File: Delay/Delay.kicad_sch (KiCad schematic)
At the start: 14 parts, among them J1 9V battery, J2 DC IN, J4 IN, J5 OUT, U1 PT2399

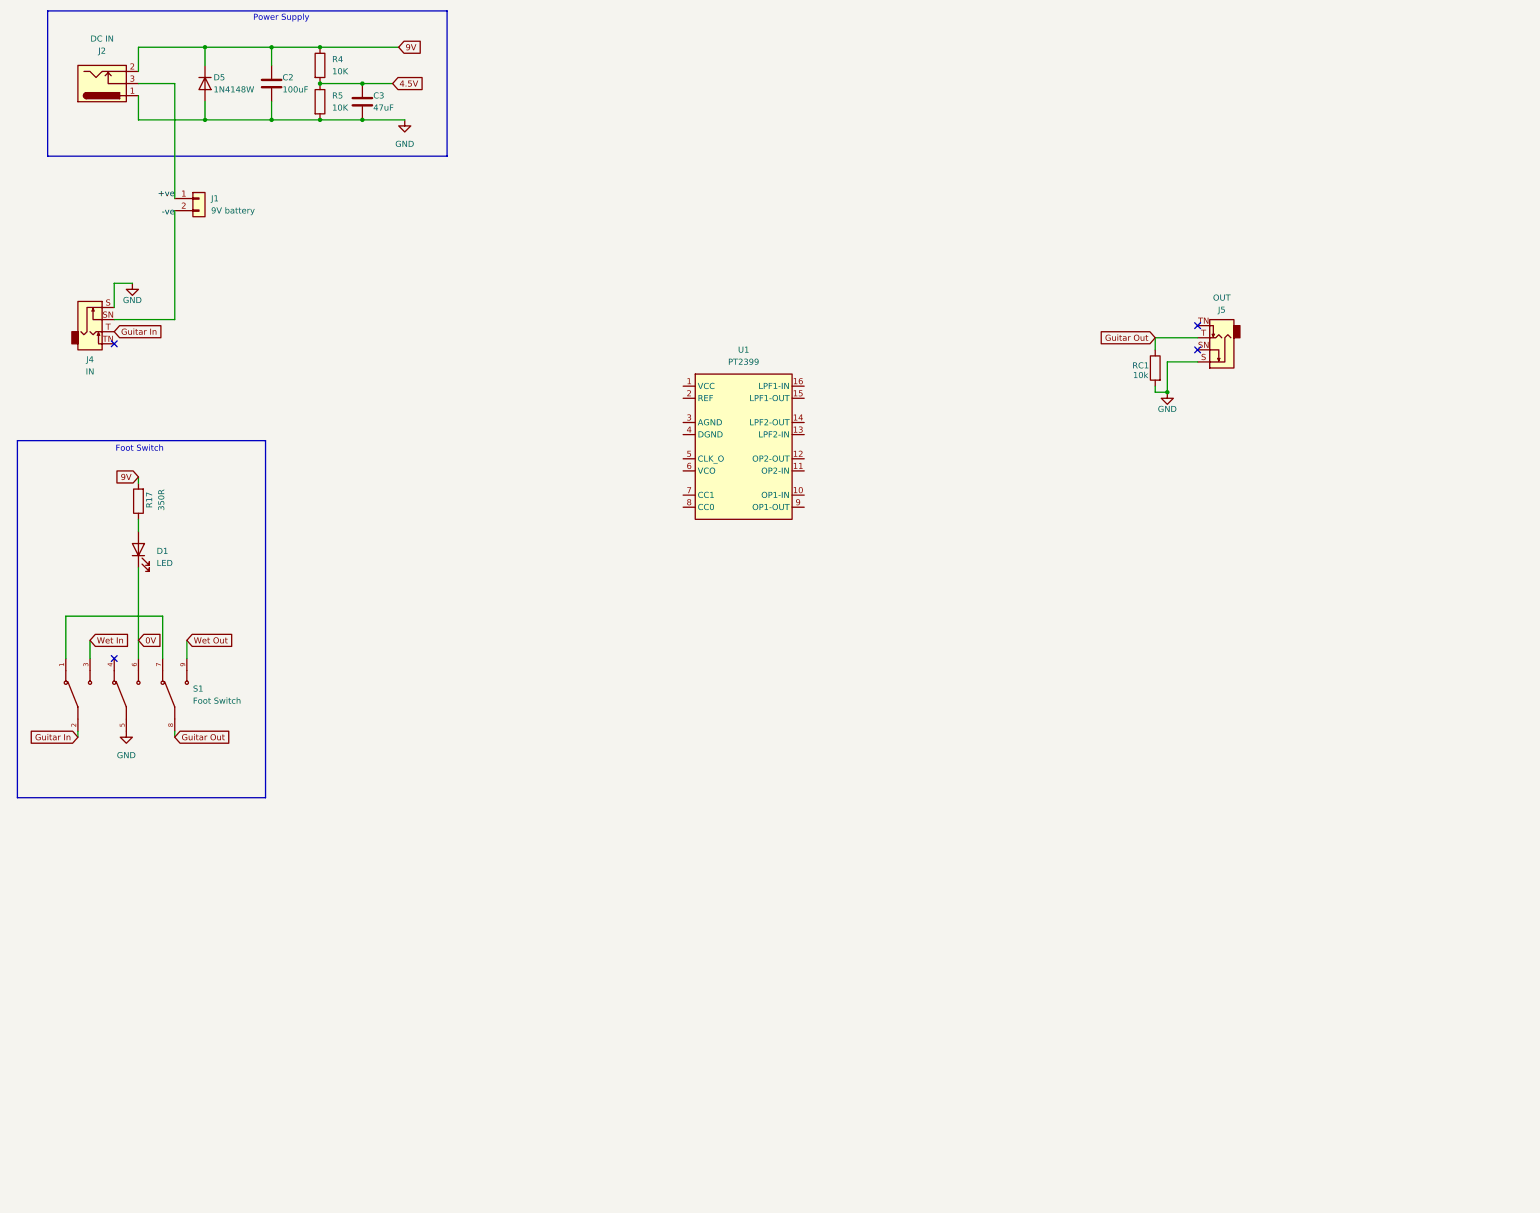
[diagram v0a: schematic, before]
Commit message: Schematic Complete. Need to finalise footprints and PCB layout.
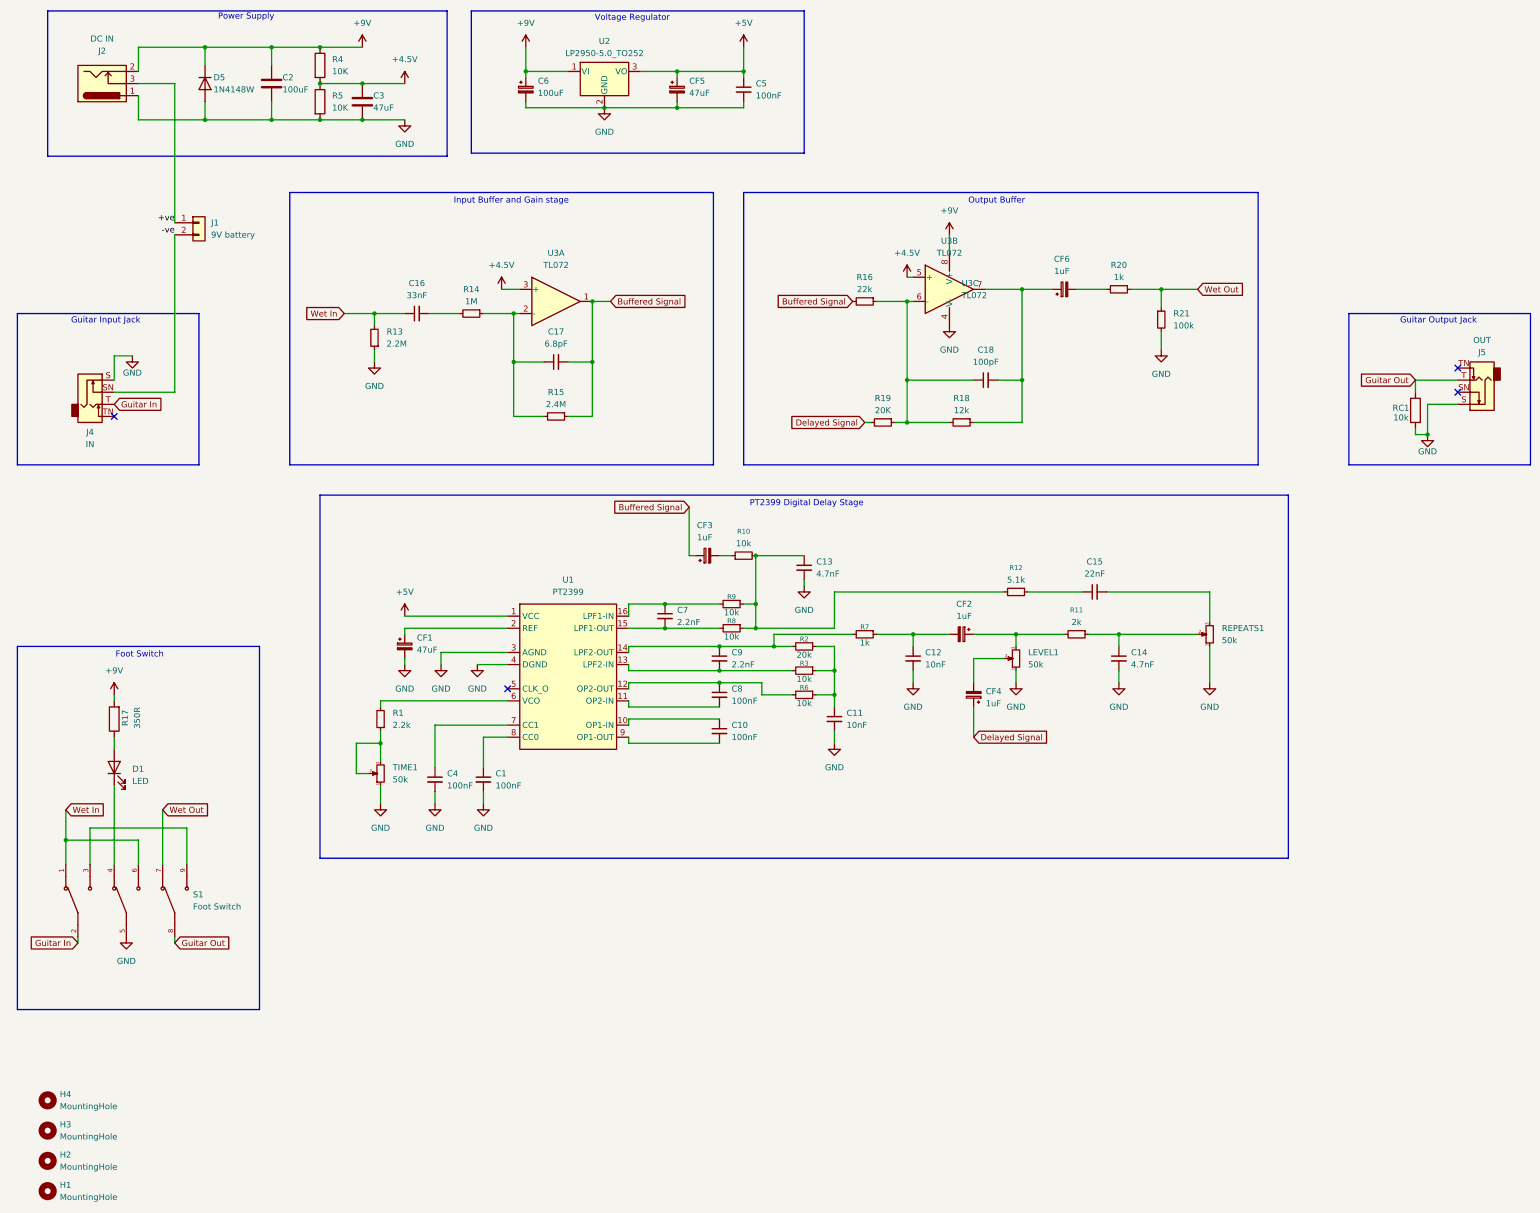
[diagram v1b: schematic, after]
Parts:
- added C1, C10, C4, C5, C8: 100nF, Capacitor_SMD:C_0805_2012Metric, symbol Device:C_Small
- added C11, C12: 10nF, Capacitor_SMD:C_0805_2012Metric, symbol Device:C_Small
- added C13, C14: 4.7nF, Capacitor_SMD:C_0805_2012Metric, symbol Device:C_Small
- added C15: 22nF, Capacitor_SMD:C_0805_2012Metric, symbol Device:C_Small
- added C16: 33nF, Capacitor_SMD:C_0805_2012Metric, symbol Device:C_Small
- added C17: 6.8pF, Capacitor_SMD:C_0805_2012Metric, symbol Device:C_Small
- added C18: 100pF, Capacitor_SMD:C_0805_2012Metric, symbol Device:C_Small
- added C6: 100uF, Capacitor_SMD:C_1206_3216Metric, symbol Device:C_Polarized_Small
- added C7, C9: 2.2nF, Capacitor_SMD:C_0805_2012Metric, symbol Device:C_Small
- added CF1, CF5: 47uF, Capacitor_SMD:CP_Elec_5x3, symbol Device:C_Polarized_Small
- added CF2, CF3, CF4, CF6: 1uF, Capacitor_SMD:CP_Elec_5x3, symbol Device:C_Polarized_Small
- added H1, H2, H3, H4: MountingHole, MountingHole:MountingHole_3.2mm_M3, symbol Mechanical:MountingHole
- added LEVEL1, REPEATS1, TIME1: 50k, Potentiometer_THT:Potentiometer_RK097_Single_Vertical, symbol Device:R_Potentiometer_Small
- added R1: 2.2k, Resistor_SMD:R_0603_1608Metric, symbol Device:R_Small
- added R10, R3, R6, R8, R9: 10k, Resistor_SMD:R_0603_1608Metric, symbol Device:R_Small
- added R11: 2k, Resistor_SMD:R_0603_1608Metric, symbol Device:R_Small
- added R12: 5.1k, Resistor_SMD:R_0603_1608Metric, symbol Device:R_Small
- added R13: 2.2M, Resistor_SMD:R_0603_1608Metric, symbol Device:R_Small
- added R14: 1M, Resistor_SMD:R_0603_1608Metric, symbol Device:R_Small
- added R15: 2.4M, Resistor_SMD:R_0603_1608Metric, symbol Device:R_Small
- added R16: 22k, Resistor_SMD:R_0603_1608Metric, symbol Device:R_Small
- added R18: 12k, Resistor_SMD:R_0603_1608Metric, symbol Device:R_Small
- added R19: 20K, Resistor_SMD:R_0603_1608Metric, symbol Device:R_Small
- added R2: 20k, Resistor_SMD:R_0603_1608Metric, symbol Device:R_Small
- added R20, R7: 1k, Resistor_SMD:R_0603_1608Metric, symbol Device:R_Small
- added R21: 100k, Resistor_SMD:R_0603_1608Metric, symbol Device:R_Small
- added U2: LP2950-5.0_TO252, Package_TO_SOT_SMD:TO-252-2, symbol Regulator_Linear:LP2950-5.0_TO252
- added U3: TL072, Package_SO:SOIC-8_5.3x6.2mm_P1.27mm, symbol Amplifier_Operational:TL072
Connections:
- net GND: now also U1.3 (AGND), U1.4 (DGND), C1.2, C11.2, C12.2, C13.2, C14.2, C4.2, C5.2, C6.2, CF1.2, CF5.2, LEVEL1.1, R13.1, R21.2, REPEATS1.1, TIME1.1, U2.2 (GND), U3.4 (V-)
- net Wet In: now also S1.1, S1.6, C16.1, R13.2; no longer S1.3
- net Wet Out: now also S1.7, R20.1, R21.1; no longer S1.9
- net at S1.4: now also D1.1 (K)
- net +5V: now reaches U1.1 (VCC)
- net +5V: now also C5.1, CF5.1, U2.3 (VO)
- net at U1.10 (OP1-IN): now also C10.1
- net at U1.11 (OP2-IN): now also C8.2
- net at U1.12 (OP2-OUT): now also C8.1, R6.2
- net at U1.13 (LPF2-IN): now also C9.2, R3.2
- net at U1.14 (LPF2-OUT): now also C9.1, R2.2, R7.2
- net at U1.15 (LPF1-OUT): now also C7.2, R8.2
- net at U1.16 (LPF1-IN): now also C7.1, R9.2
- net at U1.2 (REF): now also CF1.1
- net at U1.6 (VCO): now also R1.2
- net at U1.7 (CC1): now also C4.1
- net at U1.8 (CC0): now also C1.1
- net at U1.9 (OP1-OUT): now also C10.2
- removed net 0V: D1.1 (K), S1.6
- net 4.5V renamed +4.5V
- net +4.5V: now also U3.3 (+), U3.5 (+)
- net 9V renamed +9V
- net +9V: now also C6.1, U2.1 (VI), U3.8 (V+)
- new net: CF4.2, LEVEL1.2
- new net: CF2.1, LEVEL1.3, R11.2
- new net: C18.2, CF6.1, R18.1, U3.7
- new net: C18.1, R16.1, R18.2, R19.1, U3.6 (-)
- new net: C13.1, R10.2, R12.2, R8.1, R9.1
- new net: C14.1, R11.1, REPEATS1.2
- new net: C17.1, R14.1, R15.2, U3.2 (-)
- new net: C16.2, R14.2
- new net: C11.1, R2.1, R3.1, R6.1
- new net: R1.1, TIME1.2, TIME1.3
- new net: C15.1, R12.1
- new net: CF6.2, R20.2
- new net: C15.2, REPEATS1.3
- new net: CF3.2, R10.1
- new net: C12.1, CF2.2, R7.1
- new net: S1.3, S1.9
- new net Buffered Signal: C17.2, CF3.1, R15.1, R16.2, U3.1
- new net Delayed Signal: CF4.1, R19.2
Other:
- note added: "Guitar Input Jack"
- note added: "Guitar Output Jack"
- note added: "Input Buffer and Gain stage"
- note added: "Output Buffer"
- note added: "PT2399 Digital Delay Stage"
- note added: "Voltage Regulator"
- title: (none) -> Delay
- moved on the sheet: D1, J1, J4, J5, R17, RC1, S1, U1

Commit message: Completed PCB layout, still need to finish BOM.
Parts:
- removed J1: 9V battery, Connector_PinSocket_2.00mm:PinSocket_1x02_P2.00mm_Vertical, symbol Connector_Generic:Conn_01x02
- added +9VBATT1: 9V Batt +ve, TestPoint:TestPoint_THTPad_2.5x2.5mm_Drill1.2mm, symbol Connector:TestPoint
- added -9VBATT1: 9V Batt -ve, TestPoint:TestPoint_THTPad_2.5x2.5mm_Drill1.2mm, symbol Connector:TestPoint
- C3: renamed from C16; value 33nF -> 220nF
- C6: renamed from C17; value 6.8pF -> 47pF
- CF1: footprint Capacitor_SMD:CP_Elec_5x3 -> Capacitor_SMD:CP_Elec_6.3x7.7
- CF2: renamed from C6; footprint Capacitor_SMD:C_1206_3216Metric -> Capacitor_SMD:CP_Elec_6.3x7.7
- CF3: renamed from CF5; footprint Capacitor_SMD:CP_Elec_5x3 -> Capacitor_SMD:CP_Elec_6.3x7.7
- CF4: renamed from CF3; footprint Capacitor_SMD:CP_Elec_5x3 -> Capacitor_SMD:CP_Elec_4x5.4
- CF5: renamed from CF2; footprint Capacitor_SMD:CP_Elec_5x3 -> Capacitor_SMD:CP_Elec_4x5.4
- CF6: renamed from CF4; footprint Capacitor_SMD:CP_Elec_5x3 -> Capacitor_SMD:CP_Elec_4x5.4
- CF7: renamed from CF6; footprint Capacitor_SMD:CP_Elec_5x3 -> Capacitor_SMD:CP_Elec_4x5.4
- H1: renamed from H4; footprint MountingHole:MountingHole_3.2mm_M3 -> MountingHole:MountingHole_3.2mm_M3_Pad_Via
- H2: renamed from H3; footprint MountingHole:MountingHole_3.2mm_M3 -> MountingHole:MountingHole_3.2mm_M3_Pad_Via
- H3: renamed from H2; footprint MountingHole:MountingHole_3.2mm_M3 -> MountingHole:MountingHole_3.2mm_M3_Pad_Via
- H4: renamed from H1; footprint MountingHole:MountingHole_3.2mm_M3 -> MountingHole:MountingHole_3.2mm_M3_Pad_Via
- R1: renamed from R17; value 350R -> 470R
- R4: renamed from R13; value 2.2M -> 1M
- R6: renamed from R14; value 1M -> 220k
- R7: renamed from R15; value 2.4M -> 470k
- U2: renamed from U1; footprint Package_DIP:DIP-16_W7.62mm -> Package_SO:SO-16_3.9x9.9mm_P1.27mm
- renumbered C2 to C1, C5 to C11, C13 to C12, C11 to C13, C12 to C14, C18 to C15, C15 to C16, C14 to C17, C3 to C2, C1 to C5, C9 to C8, C8 to C9, D5 to D2, J4 to J1, J5 to J3, R2 to R11, R3 to R12, R6 to R13, R16 to R14, R7 to R15, R19 to R16, R18 to R17, R12 to R18, R11 to R19, R4 to R2, R5 to R3, R1 to R5, R9 to R8, R8 to R9, U3 to U1, U2 to U3
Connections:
- net +ve: no longer names the net of J2.3
- net +ve: now also +9VBATT1.1
- net -ve: no longer names the net of J1.SN
- net -ve: now also -9VBATT1.1

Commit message: Finalised PCB layout (110mmx60mm) and completed BOM (apart from C1 is only rated for 6.3V which might need to change).
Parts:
- C10, C11, C12, C13, C14, C15, C16, C17, C3, C4, C5, C6, C7, C8, C9: footprint Capacitor_SMD:C_0805_2012Metric -> Capacitor_SMD:C_0603_1608Metric
- C2: footprint Capacitor_SMD:C_0805_2012Metric -> Capacitor_SMD:C_1206_3216Metric
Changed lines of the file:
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@@
 			)
 		)
-		(property "Footprint" "Capacitor_SMD:C_0805_2012Metric"
+		(property "Footprint" "Capacitor_SMD:C_0603_1608Metric"
 			(at 166.37 168.91 0)
 			(effects
@@
 			)
 		)
-		(property "Footprint" "Capacitor_SMD:C_0805_2012Metric"
+		(property "Footprint" "Capacitor_SMD:C_0603_1608Metric"
 			(at 116.84 186.69 0)
 			(effects
@@
 			)
 		)
-		(property "Footprint" "Capacitor_SMD:C_0805_2012Metric"
+		(property "Footprint" "Capacitor_SMD:C_0603_1608Metric"
 			(at 184.15 142.24 0)
 			(effects
@@
 			)
 		)
-		(property "Footprint" "Capacitor_SMD:C_0805_2012Metric"
+		(property "Footprint" "Capacitor_SMD:C_0603_1608Metric"
 			(at 245.11 147.32 0)
 			(effects
@@
 			)
 		)
-		(property "Footprint" "Capacitor_SMD:C_0805_2012Metric"
+		(property "Footprint" "Capacitor_SMD:C_0603_1608Metric"
 			(at 250.19 161.29 0)
 			(effects
@@
 			)
 		)
-		(property "Footprint" "Capacitor_SMD:C_0805_2012Metric"
+		(property "Footprint" "Capacitor_SMD:C_0603_1608Metric"
 			(at 166.37 161.29 0)
 			(effects
@@
 			)
 		)
-		(property "Footprint" "Capacitor_SMD:C_0805_2012Metric"
+		(property "Footprint" "Capacitor_SMD:C_1206_3216Metric"
 			(at 92.4052 48.26 0)
 			(effects
@@
 			)
 		)
-		(property "Footprint" "Capacitor_SMD:C_0805_2012Metric"
+		(property "Footprint" "Capacitor_SMD:C_0603_1608Metric"
 			(at 154.94 152.4 0)
 			(effects
@@
 			)
 		)
-		(property "Footprint" "Capacitor_SMD:C_0805_2012Metric"
+		(property "Footprint" "Capacitor_SMD:C_0603_1608Metric"
 			(at 132.08 99.06 0)
 			(effects
@@
 			)
 		)
-		(property "Footprint" "Capacitor_SMD:C_0805_2012Metric"
+		(property "Footprint" "Capacitor_SMD:C_0603_1608Metric"
 			(at 106.68 186.69 0)
 			(effects
@@
 			)
 		)
-		(property "Footprint" "Capacitor_SMD:C_0805_2012Metric"
+		(property "Footprint" "Capacitor_SMD:C_0603_1608Metric"
 			(at 207.01 161.29 0)
 			(effects
@@
 			)
 		)
-		(property "Footprint" "Capacitor_SMD:C_0805_2012Metric"
+		(property "Footprint" "Capacitor_SMD:C_0603_1608Metric"
 			(at 190.5 173.99 0)
 			(effects
@@
 			)
 		)
-		(property "Footprint" "Capacitor_SMD:C_0805_2012Metric"
+		(property "Footprint" "Capacitor_SMD:C_0603_1608Metric"
 			(at 166.37 176.53 0)
 			(effects
@@
 			)
 		)
-		(property "Footprint" "Capacitor_SMD:C_0805_2012Metric"
+		(property "Footprint" "Capacitor_SMD:C_0603_1608Metric"
 			(at 222.25 102.87 0)
 			(effects
@@
 			)
 		)
-		(property "Footprint" "Capacitor_SMD:C_0805_2012Metric"
+		(property "Footprint" "Capacitor_SMD:C_0603_1608Metric"
 			(at 171.45 41.91 0)
 			(effects
@@
 			)
 		)
-		(property "Footprint" "Capacitor_SMD:C_0805_2012Metric"
+		(property "Footprint" "Capacitor_SMD:C_0603_1608Metric"
 			(at 102.87 88.9 0)
 			(effects

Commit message: changed caps to be THT and to be sourced separately.
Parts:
- CF1, CF2, CF3: footprint Capacitor_SMD:CP_Elec_6.3x7.7 -> Capacitor_THT:CP_Radial_D6.3mm_P2.50mm
- CF4, CF5, CF6, CF7: footprint Capacitor_SMD:CP_Elec_4x5.4 -> Capacitor_THT:CP_Radial_D5.0mm_P2.50mm
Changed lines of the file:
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@@
 			)
 		)
-		(property "Footprint" "Capacitor_SMD:CP_Elec_4x5.4"
+		(property "Footprint" "Capacitor_THT:CP_Radial_D5.0mm_P2.50mm"
 			(at 238.76 83.82 0)
 			(effects
@@
 			)
 		)
-		(property "Footprint" "Capacitor_SMD:CP_Elec_4x5.4"
+		(property "Footprint" "Capacitor_THT:CP_Radial_D5.0mm_P2.50mm"
 			(at 163.83 139.7 0)
 			(effects
@@
 			)
 		)
-		(property "Footprint" "Capacitor_SMD:CP_Elec_6.3x7.7"
+		(property "Footprint" "Capacitor_THT:CP_Radial_D6.3mm_P2.50mm"
 			(at 125.73 41.91 0)
 			(effects
@@
 			)
 		)
-		(property "Footprint" "Capacitor_SMD:CP_Elec_6.3x7.7"
+		(property "Footprint" "Capacitor_THT:CP_Radial_D6.3mm_P2.50mm"
 			(at 100.33 158.75 0)
 			(effects
@@
 			)
 		)
-		(property "Footprint" "Capacitor_SMD:CP_Elec_4x5.4"
+		(property "Footprint" "Capacitor_THT:CP_Radial_D5.0mm_P2.50mm"
 			(at 219.71 168.91 0)
 			(effects
@@
 			)
 		)
-		(property "Footprint" "Capacitor_SMD:CP_Elec_4x5.4"
+		(property "Footprint" "Capacitor_THT:CP_Radial_D5.0mm_P2.50mm"
 			(at 217.17 156.21 0)
 			(effects
@@
 			)
 		)
-		(property "Footprint" "Capacitor_SMD:CP_Elec_6.3x7.7"
+		(property "Footprint" "Capacitor_THT:CP_Radial_D6.3mm_P2.50mm"
 			(at 157.48 41.91 0)
 			(effects
